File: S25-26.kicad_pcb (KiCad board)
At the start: 6 copper layers, 90 x 90 mm, 156 parts, among them IC1 CMV4000-3E5M0PN, IC10 DS90LV048ATM_NOPB, IC2 MXL86110I-AQB-R, IC3 TPS5430DDAR, IC4 MT29F2G01ABAGDWB-IT_G_TR, IC5 MT29F2G01ABAGDWB-IT_G_TR, IC6 XMC7200D-E272K8384AA, IC7 DS90LV011AHMF_NOPB, IC8 DS90LV048ATM_NOPB, IC9 DS90LV048ATM_NOPB, J1 DC_IN_PADS, J2 Conn_01x06_Pin, J3 Conn_01x04_Pin, J4 RJ45_JXD1-0001NL, J5 Conn_01x04_Pin, Q1 ZXT849K, U1 TPS73601MDBVREP, U2 TPS73601MDBVREP, Y1 DSC1101DM2-012.0000, Y2 DSC1101DM2-125.0000T

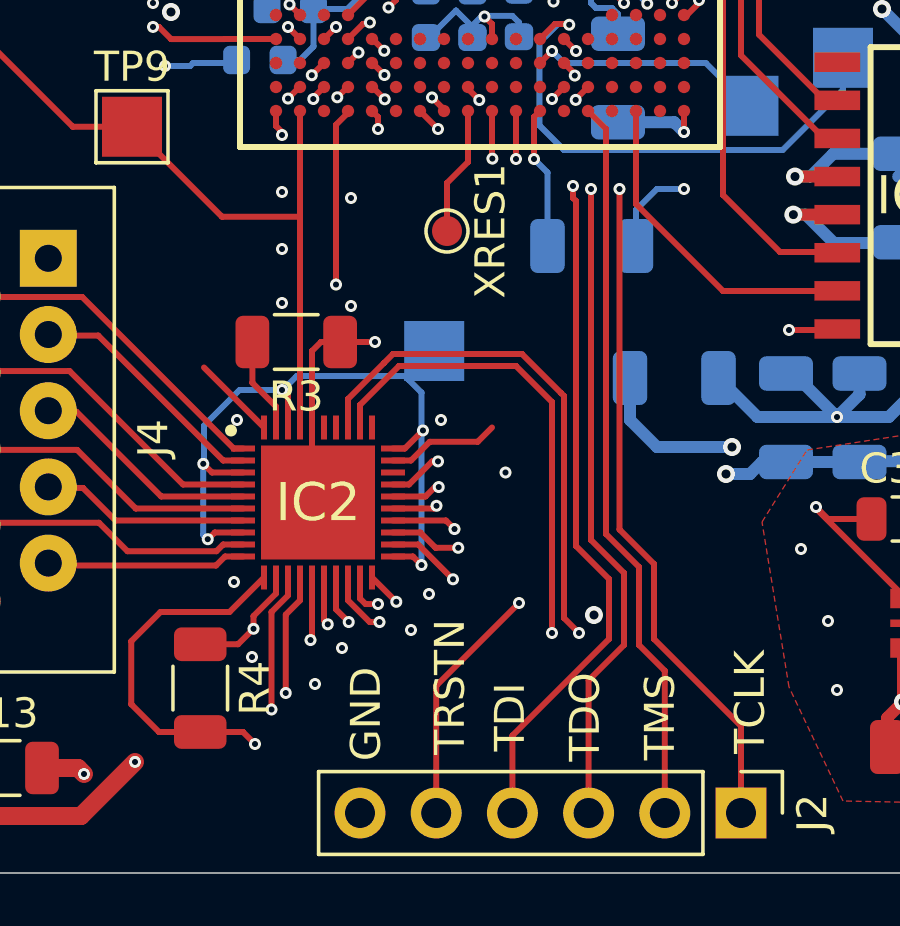
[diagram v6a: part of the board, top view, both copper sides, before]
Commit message: Ready to order
Still unsure about 100uF cap
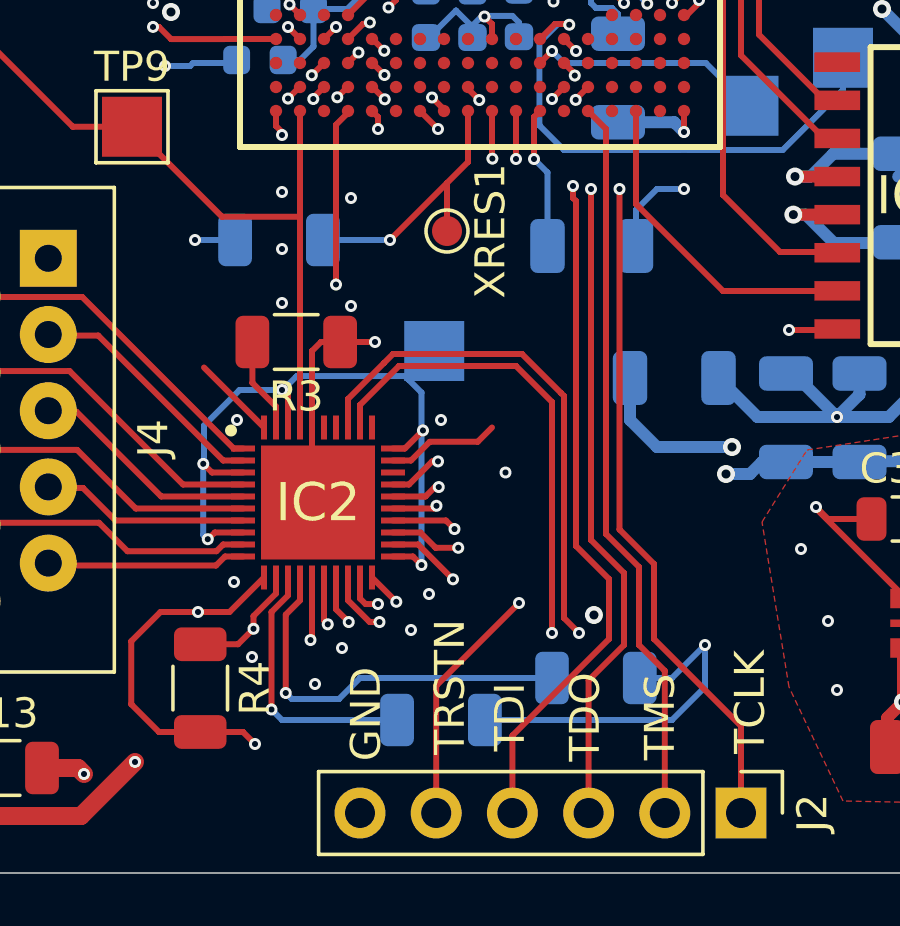
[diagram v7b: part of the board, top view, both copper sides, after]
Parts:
- added R14: 10k, Resistor_SMD:R_1206_3216Metric, B.Cu at (136.3, 119.1)
- added R15: 10k, Resistor_SMD:R_1206_3216Metric, B.Cu at (141.7, 135.1)
- added R16: 10k, Resistor_SMD:R_1206_3216Metric, B.Cu at (146.9, 133.7)
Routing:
- net +3V3: track 540.6 -> 566.8 mm, vias 32 -> 35
- net /ETH0_MDIO: track 35.6 -> 44.8 mm
- net Net-(IC6B-XRES__L): track 4.29 -> 9.21 mm, vias 0 -> 1
- net /ETH0_MDC: track 39.5 -> 43.9 mm
